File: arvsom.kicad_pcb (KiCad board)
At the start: 12 copper layers, 55 x 40 mm, 11 parts, among them J3 DF40C-100DP-0.4V(51), J4 DF40C-100DP-0.4V(51), U1 MT53D1024M32D4DT-053, U10 TDA19988BHN_C1,557, U11 KSZ9031RNXCA, U13 VIC7100, U3 MT53D1024M32D4DT-053, U8 TPS65086100, U9 GD25LQ256DWIGR

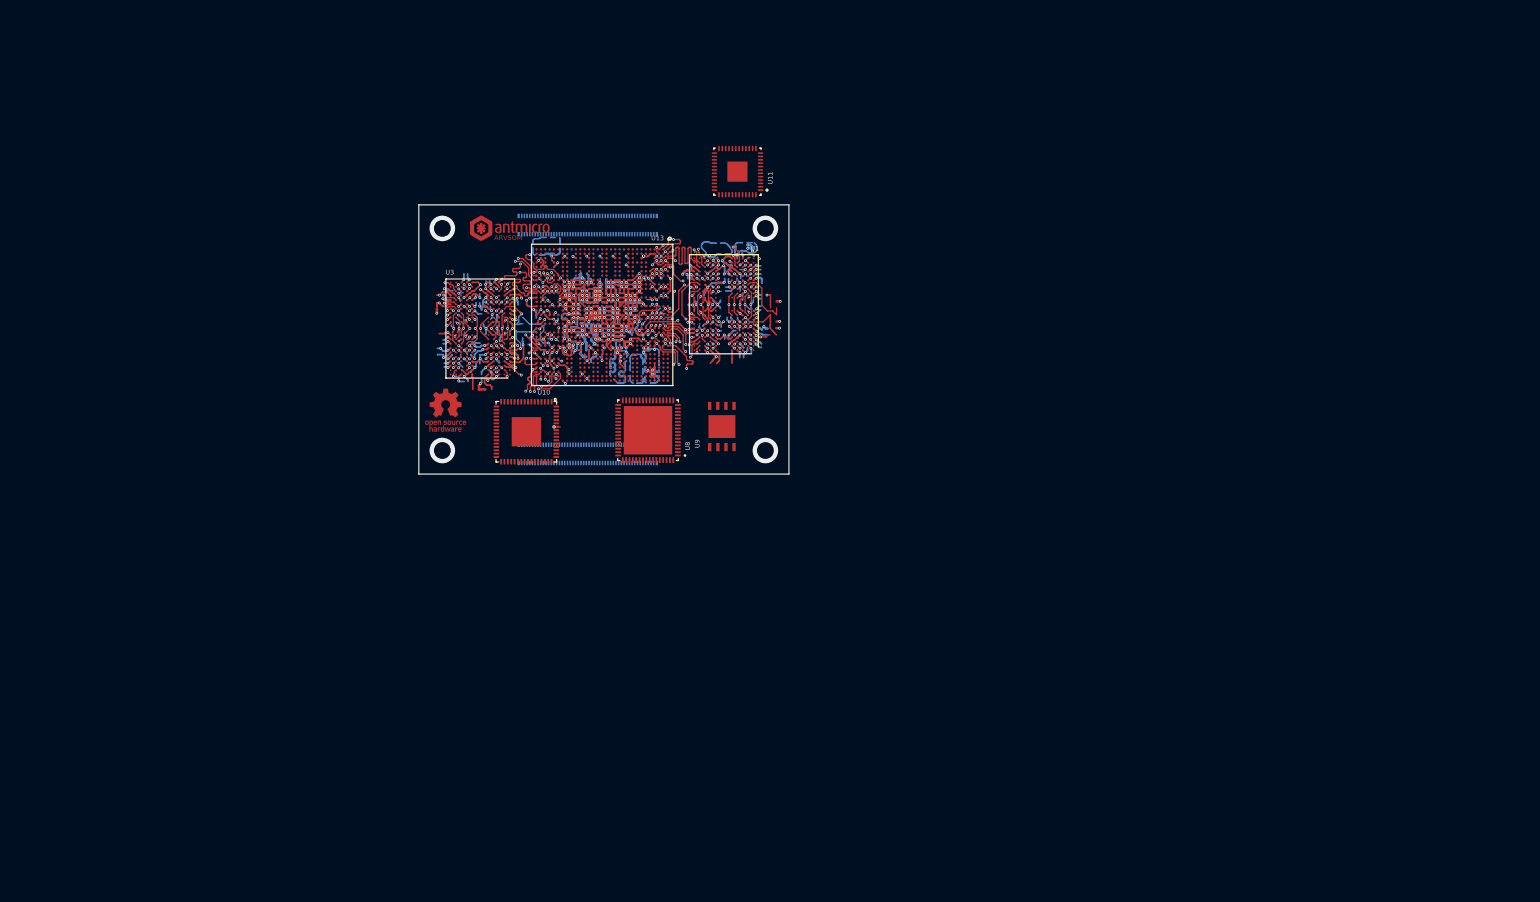
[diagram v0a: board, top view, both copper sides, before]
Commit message: Added basic rules, removed lefover zones, imported components
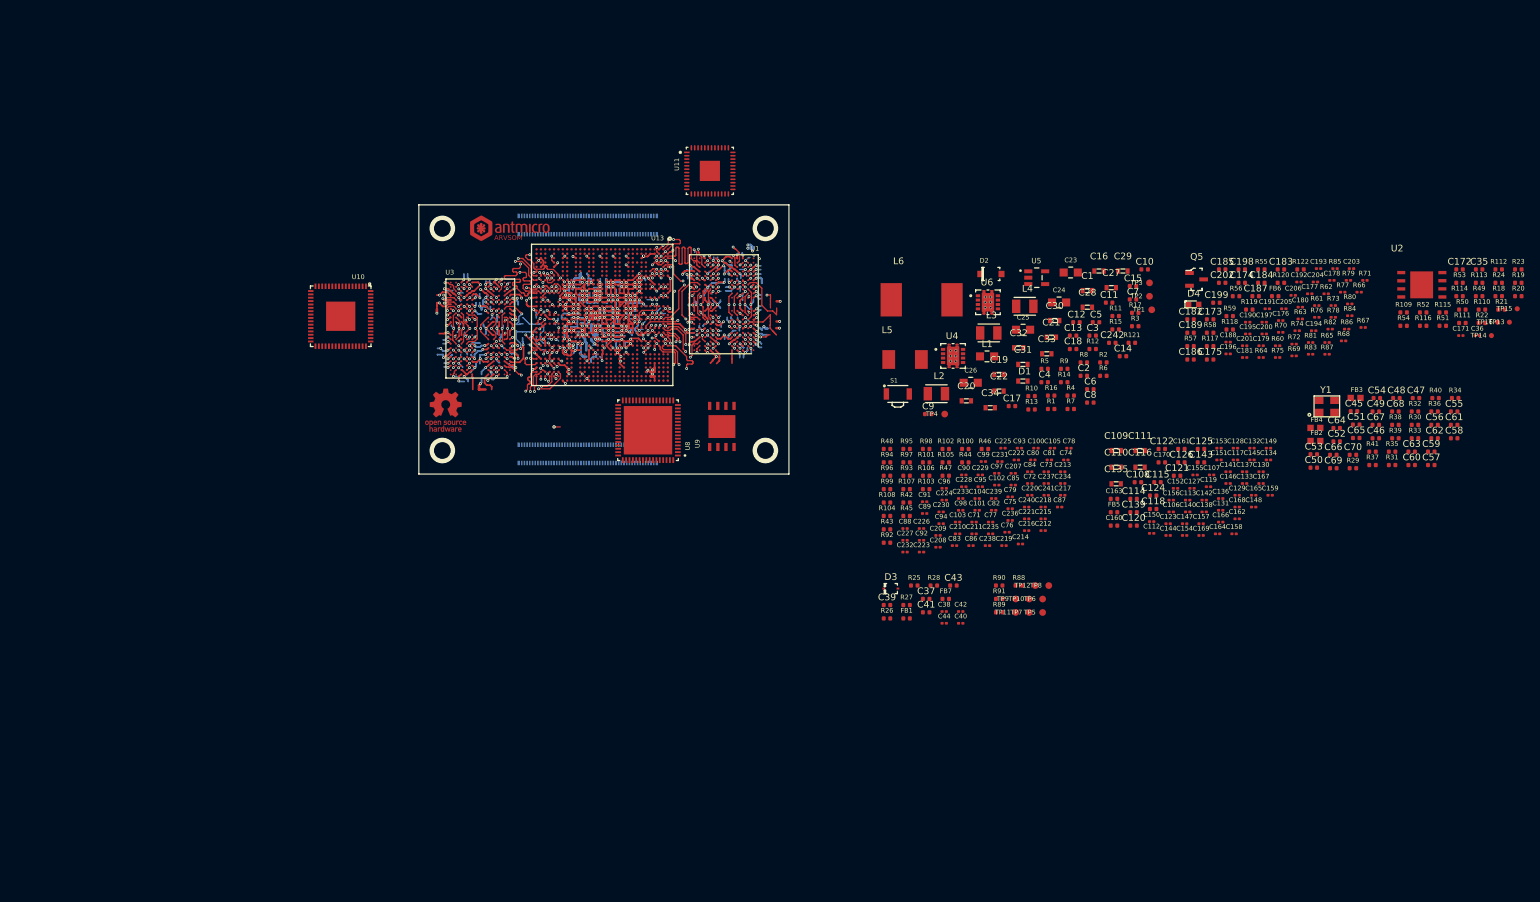
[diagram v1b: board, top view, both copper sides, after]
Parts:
- added C1: C_10u_0603, arvsom-footprints:0603-cap, F.Cu at (229.4, 67.7)
- added C10: C_100n_0402_16V, arvsom-footprints:0402-cap, F.Cu at (237.9, 64.6)
- added C100: C_100n_0201, arvsom-footprints:0201-res, F.Cu at (221.7, 91.1)
- added C101: C_100n_0201, arvsom-footprints:0201-res, F.Cu at (213.0, 100.3)
- added C102: C_100n_0201, arvsom-footprints:0201-res, F.Cu at (215.9, 96.6)
- added C103: C_100n_0201, arvsom-footprints:0201-res, F.Cu at (210.1, 102.1)
- added C104: C_100n_0201, arvsom-footprints:0201-res, F.Cu at (213.0, 98.6)
- added C105: C_100n_0201, arvsom-footprints:0201-res, F.Cu at (224.2, 91.1)
- added C106: C_100n_0201, arvsom-footprints:0201-res, F.Cu at (241.8, 100.6)
- added C107: C_100n_0201, arvsom-footprints:0201-res, F.Cu at (247.8, 95.1)
- added C108: C_1u_0402, arvsom-footprints:0402-cap, F.Cu at (236.9, 96.2)
- added C109: C_22u_0603, arvsom-footprints:0603-cap, F.Cu at (233.6, 91.5)
- added C11: C_4u7_0402, arvsom-footprints:0402-cap, F.Cu at (232.6, 69.5)
- added C110: C_22u_0603, arvsom-footprints:0603-cap, F.Cu at (233.6, 94.0)
- added C111: C_22u_0603, arvsom-footprints:0603-cap, F.Cu at (237.2, 91.5)
- added C112: C_100n_0201, arvsom-footprints:0201-res, F.Cu at (238.9, 103.8)
- added C113: C_100n_0201, arvsom-footprints:0201-res, F.Cu at (244.3, 98.8)
- added C114: C_10u_0402, arvsom-footprints:0402-cap, F.Cu at (236.2, 98.7)
- added C115: C_10u_0402, arvsom-footprints:0402-cap, F.Cu at (239.8, 96.2)
- added C116: C_22u_0603, arvsom-footprints:0603-cap, F.Cu at (237.2, 94.0)
- added C117: C_100n_0201, arvsom-footprints:0201-res, F.Cu at (251.4, 92.9)
- added C118: C_10u_0402, arvsom-footprints:0402-cap, F.Cu at (239.1, 100.2)
- added C119: C_100n_0201, arvsom-footprints:0201-res, F.Cu at (247.4, 96.8)
- added C12: C_1n0_0402, arvsom-footprints:0402-cap, F.Cu at (227.7, 72.4)
- added C120: C_10u_0402, arvsom-footprints:0402-cap, F.Cu at (236.2, 102.6)
- added C121: C_10u_0402, arvsom-footprints:0402-cap, F.Cu at (242.7, 95.2)
- added C122: C_10u_0402, arvsom-footprints:0402-cap, F.Cu at (240.4, 91.2)
- added C123: C_100n_0201, arvsom-footprints:0201-res, F.Cu at (241.4, 102.3)
- added C124: C_1u_0402, arvsom-footprints:0402-cap, F.Cu at (239.1, 98.2)
- added C125: C_1u_0402, arvsom-footprints:0402-cap, F.Cu at (246.2, 91.2)
- added C126: C_1u_0402, arvsom-footprints:0402-cap, F.Cu at (243.3, 93.2)
- added C127: C_100n_0201, arvsom-footprints:0201-res, F.Cu at (244.9, 97.1)
- added C128: C_100n_0201, arvsom-footprints:0201-res, F.Cu at (251.4, 91.1)
- added C129: C_100n_0201, arvsom-footprints:0201-res, F.Cu at (251.6, 98.1)
- added C13: C_100n_0402_16V, arvsom-footprints:0402-cap, F.Cu at (227.2, 74.4)
- added C130: C_100n_0201, arvsom-footprints:0201-res, F.Cu at (255.2, 94.6)
- added C131: C_100n_0201, arvsom-footprints:0201-res, F.Cu at (249.2, 100.3)
- added C132: C_100n_0201, arvsom-footprints:0201-res, F.Cu at (253.8, 91.1)
- added C133: C_100n_0201, arvsom-footprints:0201-res, F.Cu at (252.7, 96.4)
- added C134: C_100n_0201, arvsom-footprints:0201-res, F.Cu at (256.3, 92.9)
- added C135: C_22u_0603, arvsom-footprints:0603-cap, F.Cu at (233.6, 96.4)
- added C136: C_100n_0201, arvsom-footprints:0201-res, F.Cu at (249.2, 98.6)
- added C137: C_100n_0201, arvsom-footprints:0201-res, F.Cu at (252.7, 94.6)
- added C138: C_100n_0201, arvsom-footprints:0201-res, F.Cu at (246.7, 100.6)
- added C139: C_10u_0402, arvsom-footprints:0402-cap, F.Cu at (236.2, 100.6)
- added C14: C_4u7_0402, arvsom-footprints:0402-cap, F.Cu at (234.7, 77.5)
- added C140: C_100n_0201, arvsom-footprints:0201-res, F.Cu at (244.3, 100.6)
- added C141: C_100n_0201, arvsom-footprints:0201-res, F.Cu at (250.3, 94.6)
- added C142: C_100n_0201, arvsom-footprints:0201-res, F.Cu at (246.7, 98.8)
- added C143: C_1u_0402, arvsom-footprints:0402-cap, F.Cu at (246.2, 93.2)
- added C144: C_100n_0201, arvsom-footprints:0201-res, F.Cu at (241.4, 104.1)
- added C145: C_100n_0201, arvsom-footprints:0201-res, F.Cu at (253.8, 92.9)
- added C146: C_100n_0201, arvsom-footprints:0201-res, F.Cu at (250.3, 96.4)
- added C147: C_100n_0201, arvsom-footprints:0201-res, F.Cu at (243.8, 102.3)
- added C148: C_100n_0201, arvsom-footprints:0201-res, F.Cu at (254.1, 99.9)
- added C149: C_100n_0201, arvsom-footprints:0201-res, F.Cu at (256.3, 91.1)
- added C15: C_2u2_0402, arvsom-footprints:0402-cap, F.Cu at (236.1, 67.0)
- added C150: C_100n_0201, arvsom-footprints:0201-res, F.Cu at (238.9, 102.0)
- added C151: C_100n_0201, arvsom-footprints:0201-res, F.Cu at (248.9, 92.9)
- added C152: C_100n_0201, arvsom-footprints:0201-res, F.Cu at (242.5, 97.1)
- added C153: C_100n_0201, arvsom-footprints:0201-res, F.Cu at (248.9, 91.1)
- added C154: C_100n_0201, arvsom-footprints:0201-res, F.Cu at (243.8, 104.1)
- added C155: C_100n_0201, arvsom-footprints:0201-res, F.Cu at (245.4, 95.1)
- added C156: C_100n_0201, arvsom-footprints:0201-res, F.Cu at (241.8, 98.8)
- added C157: C_100n_0201, arvsom-footprints:0201-res, F.Cu at (246.3, 102.3)
- added C158: C_100n_0201, arvsom-footprints:0201-res, F.Cu at (251.2, 103.8)
- added C159: C_100n_0201, arvsom-footprints:0201-res, F.Cu at (256.5, 98.1)
- added C16: C_10u_0603, arvsom-footprints:0603-cap, F.Cu at (231.1, 64.8)
- added C160: C_1n_0402, arvsom-footprints:0402-res, F.Cu at (233.3, 102.6)
- added C161: C_1n_0402, arvsom-footprints:0402-res, F.Cu at (243.3, 91.2)
- added C162: C_100n_0201, arvsom-footprints:0201-res, F.Cu at (251.6, 101.6)
- added C163: C_1n_0402, arvsom-footprints:0402-res, F.Cu at (233.3, 98.7)
- added C164: C_100n_0201, arvsom-footprints:0201-res, F.Cu at (248.7, 103.8)
- added C165: C_100n_0201, arvsom-footprints:0201-res, F.Cu at (254.1, 98.1)
- added C166: C_100n_0201, arvsom-footprints:0201-res, F.Cu at (249.2, 102.1)
- added C167: C_100n_0201, arvsom-footprints:0201-res, F.Cu at (255.2, 96.4)
- added C168: C_100n_0201, arvsom-footprints:0201-res, F.Cu at (251.6, 99.9)
- added C169: C_100n_0201, arvsom-footprints:0201-res, F.Cu at (246.3, 104.1)
- added C17: C_100n_0402_16V, arvsom-footprints:0402-cap, F.Cu at (218.2, 84.9)
- added C170: C_1n_0402, arvsom-footprints:0402-res, F.Cu at (240.4, 93.2)
- added C171: C_100n_0201, arvsom-footprints:0201-res, F.Cu at (284.9, 74.4)
- added C172: C_10n_0402, arvsom-footprints:0402-cap, F.Cu at (284.7, 64.6)
- added C173: C_1u_0402, arvsom-footprints:0402-cap, F.Cu at (247.6, 72.0)
- added C174: C_1u_0402, arvsom-footprints:0402-cap, F.Cu at (252.3, 66.5)
- added C175: C_1u_0402, arvsom-footprints:0402-cap, F.Cu at (247.6, 78.0)
- added C176: C_100n_0201, arvsom-footprints:0201-res, F.Cu at (258.1, 72.2)
- added C177: C_100n_0201, arvsom-footprints:0201-res, F.Cu at (262.4, 68.2)
- added C178: C_100n_0201, arvsom-footprints:0201-res, F.Cu at (265.7, 66.2)
- added C179: C_100n_0201, arvsom-footprints:0201-res, F.Cu at (255.2, 75.9)
- added C18: C_100n_0402_16V, arvsom-footprints:0402-cap, F.Cu at (227.2, 76.4)
- added C180: C_100n_0201, arvsom-footprints:0201-res, F.Cu at (261.0, 70.2)
- added C181: C_100n_0201, arvsom-footprints:0201-res, F.Cu at (252.7, 77.7)
- added C182: C_10u_0402, arvsom-footprints:0402-cap, F.Cu at (244.7, 72.0)
- added C183: C_1u_0402, arvsom-footprints:0402-cap, F.Cu at (258.1, 64.6)
- added C184: C_10u_0402, arvsom-footprints:0402-cap, F.Cu at (255.2, 66.5)
- added C185: C_1u_0402, arvsom-footprints:0402-cap, F.Cu at (249.4, 64.6)
- added C186: C_1u_0402, arvsom-footprints:0402-cap, F.Cu at (244.7, 78.0)
- added C187: C_1u_0402, arvsom-footprints:0402-cap, F.Cu at (254.4, 68.5)
- added C188: C_100n_0201, arvsom-footprints:0201-res, F.Cu at (250.3, 75.4)
- added C189: C_1u_0402, arvsom-footprints:0402-cap, F.Cu at (244.7, 74.0)
- added C19: C_22u_0603, arvsom-footprints:0603-cap, F.Cu at (216.2, 80.2)
- added C190: C_100n_0201, arvsom-footprints:0201-res, F.Cu at (253.2, 72.4)
- added C191: C_100n_0201, arvsom-footprints:0201-res, F.Cu at (256.1, 70.4)
- added C192: C_100n_0201, arvsom-footprints:0201-res, F.Cu at (260.8, 66.4)
- added C193: C_100n_0201, arvsom-footprints:0201-res, F.Cu at (263.7, 64.4)
- added C194: C_100n_0201, arvsom-footprints:0201-res, F.Cu at (263.0, 73.7)
- added C195: C_100n_0201, arvsom-footprints:0201-res, F.Cu at (253.2, 74.2)
- added C196: C_100n_0201, arvsom-footprints:0201-res, F.Cu at (250.3, 77.1)
- added C197: C_100n_0201, arvsom-footprints:0201-res, F.Cu at (255.6, 72.4)
- added C198: C_1u_0402, arvsom-footprints:0402-cap, F.Cu at (252.3, 64.6)
- added C199: C_1u_0402, arvsom-footprints:0402-cap, F.Cu at (248.5, 69.5)
- added C2: C_2u2_0402, arvsom-footprints:0402-cap, F.Cu at (228.8, 80.4)
- added C20: C_22u_0603, arvsom-footprints:0603-cap, F.Cu at (211.4, 84.1)
- added C200: C_100n_0201, arvsom-footprints:0201-res, F.Cu at (255.6, 74.2)
- added C201: C_100n_0201, arvsom-footprints:0201-res, F.Cu at (252.7, 75.9)
- added C202: C_1u_0402, arvsom-footprints:0402-cap, F.Cu at (249.4, 66.5)
- added C203: C_100n_0201, arvsom-footprints:0201-res, F.Cu at (268.6, 64.4)
- added C204: C_100n_0201, arvsom-footprints:0201-res, F.Cu at (263.2, 66.4)
- added C205: C_100n_0201, arvsom-footprints:0201-res, F.Cu at (258.6, 70.4)
- added C206: C_100n_0201, arvsom-footprints:0201-res, F.Cu at (259.9, 68.4)
- added C207: C_100n_0201, arvsom-footprints:0201-res, F.Cu at (218.3, 94.9)
- added C208: C_100n_0201, arvsom-footprints:0201-res, F.Cu at (207.2, 105.8)
- added C209: C_100n_0201, arvsom-footprints:0201-res, F.Cu at (207.2, 104.1)
- added C21: C_22u_0603, arvsom-footprints:0603-cap, F.Cu at (224.0, 74.6)
- added C210: C_100n_0201, arvsom-footprints:0201-res, F.Cu at (210.1, 103.8)
- added C211: C_100n_0201, arvsom-footprints:0201-res, F.Cu at (212.5, 103.8)
- added C212: C_100n_0201, arvsom-footprints:0201-res, F.Cu at (222.8, 103.4)
- added C213: C_100n_0201, arvsom-footprints:0201-res, F.Cu at (225.7, 94.6)
- added C214: C_100n_0201, arvsom-footprints:0201-res, F.Cu at (219.4, 105.4)
- added C215: C_100n_0201, arvsom-footprints:0201-res, F.Cu at (222.8, 101.6)
- added C216: C_100n_0201, arvsom-footprints:0201-res, F.Cu at (220.3, 103.4)
- added C217: C_100n_0201, arvsom-footprints:0201-res, F.Cu at (225.7, 98.1)
- added C218: C_100n_0201, arvsom-footprints:0201-res, F.Cu at (222.8, 99.9)
- added C219: C_100n_0201, arvsom-footprints:0201-res, F.Cu at (217.0, 105.6)
- added C22: C_22u_0603, arvsom-footprints:0603-cap, F.Cu at (216.2, 82.6)
- added C220: C_100n_0201, arvsom-footprints:0201-res, F.Cu at (220.8, 98.1)
- added C221: C_100n_0201, arvsom-footprints:0201-res, F.Cu at (220.3, 101.6)
- added C222: C_100n_0201, arvsom-footprints:0201-res, F.Cu at (218.8, 92.9)
- added C223: C_100n_0201, arvsom-footprints:0201-res, F.Cu at (204.7, 106.6)
- added C224: C_100n_0201, arvsom-footprints:0201-res, F.Cu at (208.1, 98.8)
- added C225: C_100n_0201, arvsom-footprints:0201-res, F.Cu at (216.8, 91.1)
- added C226: C_100n_0201, arvsom-footprints:0201-res, F.Cu at (204.7, 103.1)
- added C227: C_100n_0201, arvsom-footprints:0201-res, F.Cu at (202.3, 104.8)
- added C228: C_100n_0201, arvsom-footprints:0201-res, F.Cu at (211.0, 96.8)
- added C229: C_100n_0201, arvsom-footprints:0201-res, F.Cu at (213.4, 95.1)
- added C23: C_100u_0805, arvsom-footprints:0805-cap, F.Cu at (226.9, 65.0)
- added C230: C_100n_0201, arvsom-footprints:0201-res, F.Cu at (207.6, 100.6)
- added C231: C_100n_0201, arvsom-footprints:0201-res, F.Cu at (216.4, 93.1)
- added C232: C_100n_0201, arvsom-footprints:0201-res, F.Cu at (202.3, 106.6)
- added C233: C_100n_0201, arvsom-footprints:0201-res, F.Cu at (210.5, 98.6)
- added C234: C_100n_0201, arvsom-footprints:0201-res, F.Cu at (225.7, 96.4)
- added C235: C_100n_0201, arvsom-footprints:0201-res, F.Cu at (215.0, 103.8)
- added C236: C_100n_0201, arvsom-footprints:0201-res, F.Cu at (217.9, 101.9)
- added C237: C_100n_0201, arvsom-footprints:0201-res, F.Cu at (223.2, 96.4)
- added C238: C_100n_0201, arvsom-footprints:0201-res, F.Cu at (214.5, 105.6)
- added C239: C_100n_0201, arvsom-footprints:0201-res, F.Cu at (215.4, 98.6)
- added C24: C_100u_0805, arvsom-footprints:0805-cap, F.Cu at (225.2, 69.5)
- added C240: C_100n_0201, arvsom-footprints:0201-res, F.Cu at (220.3, 99.9)
- added C241: C_100n_0201, arvsom-footprints:0201-res, F.Cu at (223.2, 98.1)
- added C242: C_100n_0402_16V, arvsom-footprints:0402-cap, F.Cu at (233.1, 75.5)
- added C25: C_100u_0805, arvsom-footprints:0805-cap, F.Cu at (219.8, 73.5)
- added C26: C_100u_0805, arvsom-footprints:0805-cap, F.Cu at (212.0, 81.4)
- added C27: C_10u_0603, arvsom-footprints:0603-cap, F.Cu at (232.9, 67.3)
- added C28: C_10u_0603, arvsom-footprints:0603-cap, F.Cu at (229.4, 70.2)
- added C29: C_22u_0603, arvsom-footprints:0603-cap, F.Cu at (234.6, 64.8)
- added C3: C_10u_0402, arvsom-footprints:0402-cap, F.Cu at (230.2, 74.4)
- added C30: C_22u_0603, arvsom-footprints:0603-cap, F.Cu at (224.5, 72.2)
- added C31: C_22u_0603, arvsom-footprints:0603-cap, F.Cu at (219.8, 78.7)
- added C32: C_22u_0603, arvsom-footprints:0603-cap, F.Cu at (219.2, 76.2)
- added C33: C_22u_0603, arvsom-footprints:0603-cap, F.Cu at (223.3, 77.1)
- added C34: C_22u_0603, arvsom-footprints:0603-cap, F.Cu at (214.9, 85.1)
- added C35: C_1u_0402, arvsom-footprints:0402-cap, F.Cu at (287.6, 64.6)
- added C36: C_100n_0201, arvsom-footprints:0201-res, F.Cu at (287.3, 74.4)
- added C37: C_2u2_0402, arvsom-footprints:0402-cap, F.Cu at (205.4, 113.5)
- added C38: C_100n_0201, arvsom-footprints:0201-res, F.Cu at (208.1, 115.4)
- added C39: C_2u2_0402, arvsom-footprints:0402-cap, F.Cu at (199.6, 114.4)
- added C4: C_10u_0402, arvsom-footprints:0402-cap, F.Cu at (223.0, 81.3)
- added C40: C_100n_0201, arvsom-footprints:0201-res, F.Cu at (210.5, 117.1)
- added C41: C_2u2_0402, arvsom-footprints:0402-cap, F.Cu at (205.4, 115.5)
- added C42: C_100n_0201, arvsom-footprints:0201-res, F.Cu at (210.5, 115.4)
- added C43: C_2u2_0402, arvsom-footprints:0402-cap, F.Cu at (209.5, 111.5)
- added C44: C_100n_0201, arvsom-footprints:0201-res, F.Cu at (208.1, 117.1)
- added C45: C_4u7_0402, arvsom-footprints:0402-cap, F.Cu at (269.0, 85.6)
- added C46: C_470n_0402, arvsom-footprints:0402-cap, F.Cu at (272.2, 89.7)
- added C47: C_4u7_0402, arvsom-footprints:0402-cap, F.Cu at (278.2, 83.7)
- added C48: C_470n_0402, arvsom-footprints:0402-cap, F.Cu at (275.3, 83.7)
- added C49: C_4u7_0402, arvsom-footprints:0402-cap, F.Cu at (272.2, 85.7)
- added C5: C_2u2_0402, arvsom-footprints:0402-cap, F.Cu at (230.7, 72.4)
- added C50: C_4u7_0402, arvsom-footprints:0402-cap, F.Cu at (263.0, 94.0)
- added C51: C_470n_0402, arvsom-footprints:0402-cap, F.Cu at (269.3, 87.6)
- added C52: C_470n_0402, arvsom-footprints:0402-cap, F.Cu at (266.4, 90.1)
- added C53: C_470n_0402, arvsom-footprints:0402-cap, F.Cu at (263.0, 92.0)
- added C54: C_100n_0402, arvsom-footprints:0402-cap, F.Cu at (272.4, 83.7)
- added C55: C_10n_0402, arvsom-footprints:0402-cap, F.Cu at (283.9, 85.7)
- added C56: C_10n_0402, arvsom-footprints:0402-cap, F.Cu at (280.9, 87.7)
- added C57: C_10n_0402, arvsom-footprints:0402-cap, F.Cu at (280.5, 93.6)
- added C58: C_4u7_0402, arvsom-footprints:0402-cap, F.Cu at (283.9, 89.7)
- added C59: C_10n_0402, arvsom-footprints:0402-cap, F.Cu at (280.5, 91.6)
- added C6: C_4u7_0402, arvsom-footprints:0402-cap, F.Cu at (229.8, 82.4)
- added C60: C_10n_0402, arvsom-footprints:0402-cap, F.Cu at (277.6, 93.6)
- added C61: C_10n_0402, arvsom-footprints:0402-cap, F.Cu at (283.9, 87.7)
- added C62: C_10n_0402, arvsom-footprints:0402-cap, F.Cu at (280.9, 89.7)
- added C63: C_10n_0402, arvsom-footprints:0402-cap, F.Cu at (277.6, 91.6)
- added C64: C_10n_0402, arvsom-footprints:0402-cap, F.Cu at (266.4, 88.1)
- added C65: C_10n_0402, arvsom-footprints:0402-cap, F.Cu at (269.3, 89.6)
- added C66: C_10n_0402, arvsom-footprints:0402-cap, F.Cu at (265.9, 92.1)
- added C67: C_10n_0402, arvsom-footprints:0402-cap, F.Cu at (272.2, 87.7)
- added C68: C_10n_0402, arvsom-footprints:0402-cap, F.Cu at (275.1, 85.7)
- added C69: C_22p_0402, arvsom-footprints:0402-cap, F.Cu at (265.9, 94.1)
- added C7: C_2u2_0402, arvsom-footprints:0402-cap, F.Cu at (236.1, 69.0)
- added C70: C_22p_0402, arvsom-footprints:0402-cap, F.Cu at (268.8, 92.1)
- added C71: C_100n_0201, arvsom-footprints:0201-res, F.Cu at (212.5, 102.1)
- added C72: C_100n_0201, arvsom-footprints:0201-res, F.Cu at (220.8, 96.4)
- added C73: C_100n_0201, arvsom-footprints:0201-res, F.Cu at (223.2, 94.6)
- added C74: C_100n_0201, arvsom-footprints:0201-res, F.Cu at (226.2, 92.9)
- added C75: C_100n_0201, arvsom-footprints:0201-res, F.Cu at (217.9, 100.1)
- added C76: C_100n_0201, arvsom-footprints:0201-res, F.Cu at (217.4, 103.6)
- added C77: C_100n_0201, arvsom-footprints:0201-res, F.Cu at (215.0, 102.1)
- added C78: C_100n_0201, arvsom-footprints:0201-res, F.Cu at (226.6, 91.1)
- added C79: C_100n_0201, arvsom-footprints:0201-res, F.Cu at (217.9, 98.4)
- added C8: C_10u_0402, arvsom-footprints:0402-cap, F.Cu at (229.8, 84.3)
- added C80: C_100n_0201, arvsom-footprints:0201-res, F.Cu at (221.3, 92.9)
- added C81: C_100n_0201, arvsom-footprints:0201-res, F.Cu at (223.7, 92.9)
- added C82: C_100n_0201, arvsom-footprints:0201-res, F.Cu at (215.4, 100.3)
- added C83: C_100n_0201, arvsom-footprints:0201-res, F.Cu at (209.6, 105.6)
- added C84: C_100n_0201, arvsom-footprints:0201-res, F.Cu at (220.8, 94.6)
- added C85: C_100n_0201, arvsom-footprints:0201-res, F.Cu at (218.3, 96.6)
- added C86: C_100n_0201, arvsom-footprints:0201-res, F.Cu at (212.1, 105.6)
- added C87: C_100n_0201, arvsom-footprints:0201-res, F.Cu at (225.2, 99.9)
- added C88: C_100n_0201, arvsom-footprints:0201-res, F.Cu at (202.3, 103.1)
- added C89: C_100n_0201, arvsom-footprints:0201-res, F.Cu at (205.2, 100.8)
- added C9: C_2u2_0402, arvsom-footprints:0402-cap, F.Cu at (205.7, 86.0)
- added C90: C_100n_0201, arvsom-footprints:0201-res, F.Cu at (211.0, 95.1)
- added C91: C_100n_0201, arvsom-footprints:0201-res, F.Cu at (205.2, 99.1)
- added C92: C_100n_0201, arvsom-footprints:0201-res, F.Cu at (204.7, 104.8)
- added C93: C_100n_0201, arvsom-footprints:0201-res, F.Cu at (219.3, 91.1)
- added C94: C_100n_0201, arvsom-footprints:0201-res, F.Cu at (207.6, 102.3)
- added C95: C_100n_0201, arvsom-footprints:0201-res, F.Cu at (213.4, 96.8)
- added C96: C_100n_0201, arvsom-footprints:0201-res, F.Cu at (208.1, 97.1)
- added C97: C_100n_0201, arvsom-footprints:0201-res, F.Cu at (215.9, 94.9)
- added C98: C_100n_0201, arvsom-footprints:0201-res, F.Cu at (210.5, 100.3)
- added C99: C_100n_0201, arvsom-footprints:0201-res, F.Cu at (213.9, 93.1)
- added D1: PGB1010603MR, arvsom-footprints:PGB1010603MR, F.Cu at (219.8, 81.2)
- added D2: 1N4148W-TP, arvsom-footprints:SOD-123, F.Cu at (215.0, 65.2)
- added D3: 1N4148WS, arvsom-footprints:SOD-323F, F.Cu at (200.2, 112.0)
- added D4: KP-1608CGCK, arvsom-footprints:LED_0603, F.Cu at (245.2, 69.8)
- added FB1: BLM15PD121SN1D, arvsom-footprints:0402-res, F.Cu at (202.5, 116.4)
- added FB2: BLM18AG601SN1D, arvsom-footprints:0603, F.Cu at (263.2, 90.1)
- added FB3: BLM18AG601SN1D, arvsom-footprints:0603, F.Cu at (269.2, 83.7)
- added FB4: BLM18AG601SN1D, arvsom-footprints:0603, F.Cu at (263.2, 88.1)
- added FB5: BLM15PD121SN1D, arvsom-footprints:0402-res, F.Cu at (233.3, 100.6)
- added FB6: BLM15PD121SN1D, arvsom-footprints:0402-res, F.Cu at (257.3, 68.5)
- added FB7: BLM15PD121SN1D, arvsom-footprints:0402-res, F.Cu at (208.3, 113.5)
- added L1: 10uH, arvsom-footprints:0805-res, F.Cu at (214.5, 77.5)
- added L2: LQH32PN1R0NN0L, arvsom-footprints:IND_LQH32PN1R0NN0L, F.Cu at (206.9, 83.0)
- added L3: LQH32PN1R0NN0L, arvsom-footprints:IND_LQH32PN1R0NN0L, F.Cu at (214.7, 74.0)
- added L4: LQH32PN1R0NN0L, arvsom-footprints:IND_LQH32PN1R0NN0L, F.Cu at (220.1, 70.0)
- added L5: MPX1D0520LR47, arvsom-footprints:MPX1D0520LR47, F.Cu at (198.9, 76.5)
- added L6: IHLP4040DZERR56M01, arvsom-footprints:IHLP4040DZERR56M01, F.Cu at (199.3, 67.6)
- added Q5: BSS138AKA, arvsom-footprints:SOT-23-3, F.Cu at (245.6, 66.0)
- added R1: R_1M0_0402, arvsom-footprints:0402-res, F.Cu at (224.0, 85.3)
- added R10: R_0R_0402, arvsom-footprints:0402-res, F.Cu at (221.1, 83.4)
- added R100: R_0R_0402, arvsom-footprints:0402-res, F.Cu at (211.2, 91.2)
- added R101: R_10k_0402, arvsom-footprints:0402-res, F.Cu at (205.4, 93.2)
- added R102: R_0R_0402, arvsom-footprints:0402-res, F.Cu at (208.3, 91.2)
- added R103: R_10k_0402, arvsom-footprints:0402-res, F.Cu at (205.4, 97.2)
- added R104: R_10k_0402, arvsom-footprints:0402-res, F.Cu at (199.6, 101.2)
- added R105: R_10k_0402, arvsom-footprints:0402-res, F.Cu at (208.3, 93.2)
- added R106: R_10k_0402, arvsom-footprints:0402-res, F.Cu at (205.4, 95.2)
- added R107: R_10k_0402, arvsom-footprints:0402-res, F.Cu at (202.5, 97.2)
- added R108: R_10k_0402, arvsom-footprints:0402-res, F.Cu at (199.6, 99.2)
- added R109: R_10k_0402, arvsom-footprints:0402-res, F.Cu at (276.4, 71.0)
- added R11: R_0R_0402, arvsom-footprints:0402-res, F.Cu at (233.6, 71.5)
- added R110: R_10k_0402, arvsom-footprints:0402-res, F.Cu at (288.0, 70.5)
- added R111: R_10k_0402, arvsom-footprints:0402-res, F.Cu at (285.1, 72.5)
- added R112: R_10k_0402, arvsom-footprints:0402-res, F.Cu at (290.5, 64.6)
- added R113: R_10k_0402, arvsom-footprints:0402-res, F.Cu at (287.6, 66.5)
- added R114: R_10k_0402, arvsom-footprints:0402-res, F.Cu at (284.7, 68.5)
- added R115: R_10k_0402, arvsom-footprints:0402-res, F.Cu at (282.2, 71.0)
- added R116: R_10k_0402, arvsom-footprints:0402-res, F.Cu at (279.3, 72.9)
- added R117: R_2k_0402, arvsom-footprints:0402-res, F.Cu at (247.6, 76.0)
- added R118: R_2k_0402, arvsom-footprints:0402-res, F.Cu at (250.5, 73.5)
- added R119: R_33R_0402, arvsom-footprints:0402-res, F.Cu at (253.4, 70.5)
- added R12: R_0R_0402, arvsom-footprints:0402-res, F.Cu at (230.2, 76.4)
- added R120: R_1k_0402, arvsom-footprints:0402-res, F.Cu at (258.1, 66.5)
- added R121: R_10k_0402, arvsom-footprints:0402-res, F.Cu at (236.0, 75.5)
- added R122: R_10k_0402, arvsom-footprints:0402-res, F.Cu at (261.0, 64.6)
- added R13: R_4k7_0402, arvsom-footprints:0402-res, F.Cu at (221.1, 85.4)
- added R14: R_0R_0402, arvsom-footprints:0402-res, F.Cu at (225.9, 81.3)
- added R15: R_0R_0402, arvsom-footprints:0402-res, F.Cu at (233.6, 73.5)
- added R16: R_0R_0402, arvsom-footprints:0402-res, F.Cu at (224.0, 83.3)
- added R17: R_4k7_0402, arvsom-footprints:0402-res, F.Cu at (236.5, 71.0)
- added R18: R_33R_0402, arvsom-footprints:0402-res, F.Cu at (290.5, 68.5)
- added R19: R_33R_0402, arvsom-footprints:0402-res, F.Cu at (293.4, 66.5)
- added R2: R_10k_0402, arvsom-footprints:0402-res, F.Cu at (231.7, 78.4)
- added R20: R_33R_0402, arvsom-footprints:0402-res, F.Cu at (293.4, 68.5)
- added R21: R_4k7_0402, arvsom-footprints:0402-res, F.Cu at (290.9, 70.5)
- added R22: R_33R_0402, arvsom-footprints:0402-res, F.Cu at (288.0, 72.5)
- added R23: R_33R_0402, arvsom-footprints:0402-res, F.Cu at (293.4, 64.6)
- added R24: R_33R_0402, arvsom-footprints:0402-res, F.Cu at (290.5, 66.5)
- added R25: R_10k_0402, arvsom-footprints:0402-res, F.Cu at (203.6, 111.5)
- added R26: R_1k_0402, arvsom-footprints:0402-res, F.Cu at (199.6, 116.4)
- added R27: R_1k_0402, arvsom-footprints:0402-res, F.Cu at (202.5, 114.4)
- added R28: R_27k_0402, arvsom-footprints:0402-res, F.Cu at (206.6, 111.5)
- added R29: R_1k_0402, arvsom-footprints:0402-res, F.Cu at (268.8, 94.1)
- added R3: R_10k_0402, arvsom-footprints:0402-res, F.Cu at (236.5, 73.0)
- added R30: R_12k1_0402, arvsom-footprints:0402-res, F.Cu at (278.0, 87.7)
- added R31: R_10k_0402, arvsom-footprints:0402-res, F.Cu at (274.6, 93.6)
- added R32: R_10k_0402, arvsom-footprints:0402-res, F.Cu at (278.0, 85.7)
- added R33: R_10k_0402, arvsom-footprints:0402-res, F.Cu at (278.0, 89.7)
- added R34: R_10k_0402, arvsom-footprints:0402-res, F.Cu at (284.0, 83.7)
- added R35: R_10k_0402, arvsom-footprints:0402-res, F.Cu at (274.6, 91.6)
- added R36: R_10k_0402, arvsom-footprints:0402-res, F.Cu at (280.9, 85.7)
- added R37: R_4k7_0402, arvsom-footprints:0402-res, F.Cu at (271.7, 93.6)
- added R38: R_10k_0402, arvsom-footprints:0402-res, F.Cu at (275.1, 87.7)
- added R39: R_10k_0402, arvsom-footprints:0402-res, F.Cu at (275.1, 89.7)
- added R4: R_10k_0402, arvsom-footprints:0402-res, F.Cu at (226.9, 83.3)
- added R40: R_10k_0402, arvsom-footprints:0402-res, F.Cu at (281.1, 83.7)
- added R41: R_1M5_0402, arvsom-footprints:0402-res, F.Cu at (271.7, 91.6)
- added R42: R_240R_0402, arvsom-footprints:0402-res, F.Cu at (202.5, 99.2)
- added R43: R_10k_0402, arvsom-footprints:0402-res, F.Cu at (199.6, 103.2)
- added R44: R_10k_0402, arvsom-footprints:0402-res, F.Cu at (211.2, 93.2)
- added R45: R_240R_0402, arvsom-footprints:0402-res, F.Cu at (202.5, 101.2)
- added R46: R_0R_0402, arvsom-footprints:0402-res, F.Cu at (214.1, 91.2)
- added R47: R_10k_0402, arvsom-footprints:0402-res, F.Cu at (208.3, 95.2)
- added R48: R_0R_0402, arvsom-footprints:0402-res, F.Cu at (199.6, 91.2)
- added R49: R_10k_0402, arvsom-footprints:0402-res, F.Cu at (287.6, 68.5)
- added R5: R_0R_0402, arvsom-footprints:0402-res, F.Cu at (223.0, 79.3)
- added R50: R_10k_0402, arvsom-footprints:0402-res, F.Cu at (285.1, 70.5)
- added R51: R_10k_0402, arvsom-footprints:0402-res, F.Cu at (282.2, 72.9)
- added R52: R_10k_0402, arvsom-footprints:0402-res, F.Cu at (279.3, 71.0)
- added R53: R_10k_0402, arvsom-footprints:0402-res, F.Cu at (284.7, 66.5)
- added R54: R_10k_0402, arvsom-footprints:0402-res, F.Cu at (276.4, 72.9)
- added R55: R_33R_0402, arvsom-footprints:0402-res, F.Cu at (255.2, 64.6)
- added R56: R_33R_0402, arvsom-footprints:0402-res, F.Cu at (251.4, 68.5)
- added R57: R_33R_0402, arvsom-footprints:0402-res, F.Cu at (244.7, 76.0)
- added R58: R_33R_0402, arvsom-footprints:0402-res, F.Cu at (247.6, 74.0)
- added R59: R_33R_0402, arvsom-footprints:0402-res, F.Cu at (250.5, 71.5)
- added R6: R_0R_0402, arvsom-footprints:0402-res, F.Cu at (231.7, 80.4)
- added R60: R_33R_0201, arvsom-footprints:0201-res, F.Cu at (257.6, 75.9)
- added R61: R_33R_0201, arvsom-footprints:0201-res, F.Cu at (263.4, 69.9)
- added R62: R_33R_0201, arvsom-footprints:0201-res, F.Cu at (264.9, 68.2)
- added R63: R_33R_0201, arvsom-footprints:0201-res, F.Cu at (261.0, 71.9)
- added R64: R_33R_0201, arvsom-footprints:0201-res, F.Cu at (255.2, 77.7)
- added R65: R_33R_0201, arvsom-footprints:0201-res, F.Cu at (265.0, 75.4)
- added R66: R_33R_0201, arvsom-footprints:0201-res, F.Cu at (269.8, 67.9)
- added R67: R_33R_0201, arvsom-footprints:0201-res, F.Cu at (270.3, 73.2)
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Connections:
- U13 pad AJ5: DDR1_DQ31 -> (no net)
- U3 pad AB4: VDDQ -> VDD2
- U3 pad B10: VDD2 -> VDDQ
- U3 pad B8: VDD2 -> VDDQ
- U3 pad F5: VDDQ -> VDD2
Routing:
- removed copper zone on B.Cu, net (none)
- removed copper zone on In2.Cu, net (none)
- removed copper zone on In4.Cu, net (none)
- removed copper zone on In7.Cu, net (none)
- removed copper zone on In9.Cu, net (none)
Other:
- net class Default: trace_width 0.11 -> 0.127; via_dia 0.8 -> 0.4; via_drill 0.4 -> 0.2
- rule trace_min: 0.11 -> 0.127
- rule via_min_drill: 0.3 -> 0.2

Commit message: Updated PMIC components. PMIC component grouping
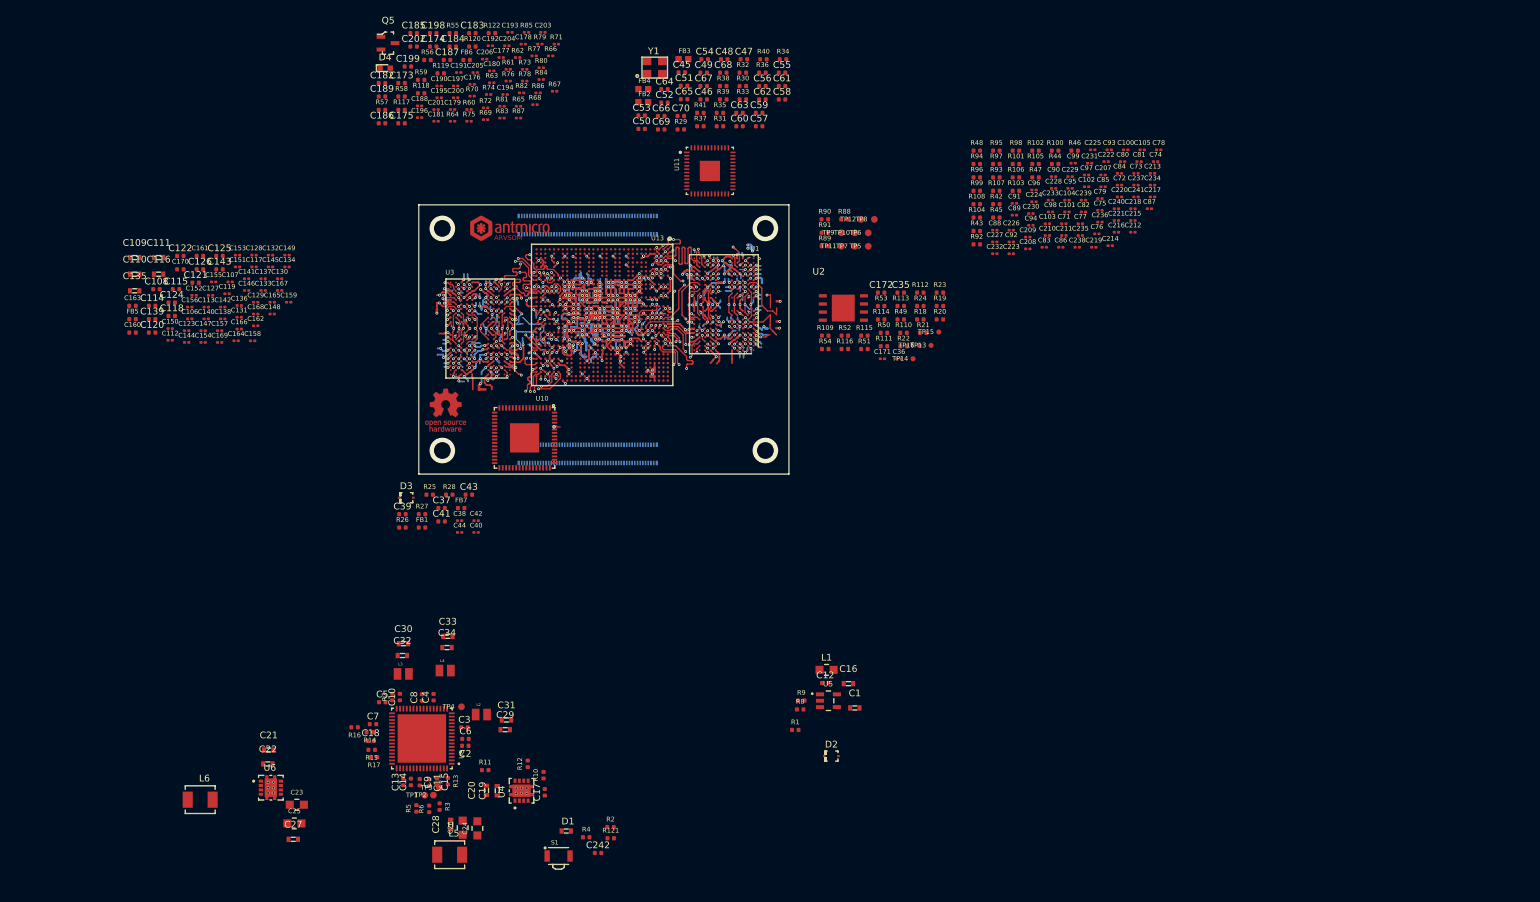
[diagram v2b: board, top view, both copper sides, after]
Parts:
- removed U9: GD25LQ256DWIGR, arvsom-footprints:8-WSON-6x5
- D2: value 1N4148W-TP -> PMEG3010CEJ; footprint arvsom-footprints:SOD-123 -> arvsom-footprints:SOD-323F
- L2, L3, L4: value LQH32PN1R0NN0L -> 1uH_2.0x1.6; footprint arvsom-footprints:IND_LQH32PN1R0NN0L -> arvsom-footprints:INDC2016X100N
- L5: value MPX1D0520LR47 -> 0.56uH_7.3A; footprint arvsom-footprints:MPX1D0520LR47 -> arvsom-footprints:SRP4020
- L6: value IHLP4040DZERR56M01 -> 0.47uH_10.5A; footprint arvsom-footprints:IHLP4040DZERR56M01 -> arvsom-footprints:SRP4020
- moved C113 148.6 mm to (98.4, 70.2)
- moved C119 148.6 mm to (101.5, 68.2)
- moved C123 148.6 mm to (95.5, 73.7)
- moved C125 148.6 mm to (100.4, 62.6)
- moved C126 148.6 mm to (97.5, 64.5)
- moved C140 148.6 mm to (98.4, 71.9)
- moved C141 148.6 mm to (104.4, 65.9)
- moved C143 148.6 mm to (100.4, 64.5)
- moved C144 148.6 mm to (95.5, 75.4)
- moved C146 148.6 mm to (104.4, 67.7)
- moved C152 148.6 mm to (96.6, 68.4)
- moved C161 148.6 mm to (97.5, 62.6)
- moved C164 148.6 mm to (102.9, 75.2)
- moved C106 148.6 mm to (96.0, 71.9)
- moved C107 148.6 mm to (102.0, 66.4)
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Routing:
- net LCD_DATA5: track 0.94 -> 0.00 mm, vias 1 -> 0
- net LCD_DATA3: track 0.00 -> 0.94 mm, vias 0 -> 1

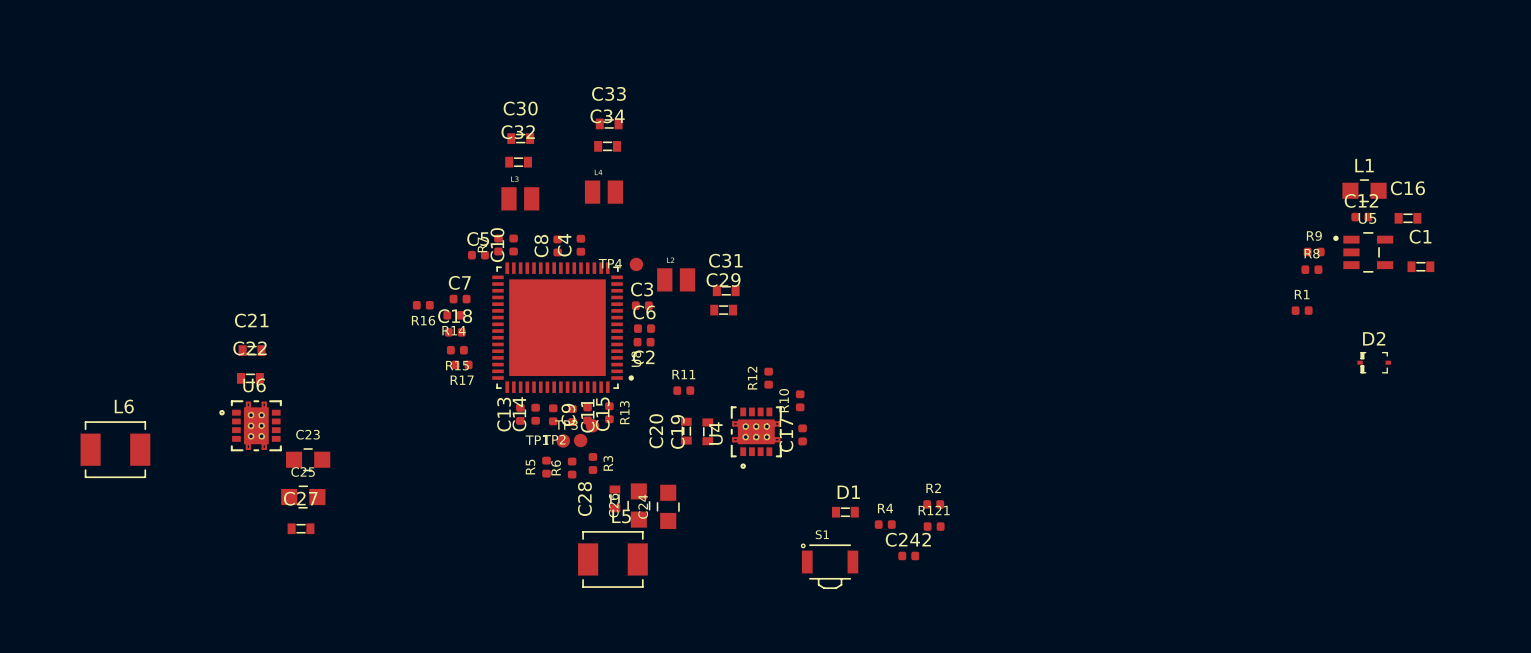
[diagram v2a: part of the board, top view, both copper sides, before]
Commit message: Started PMIC placement
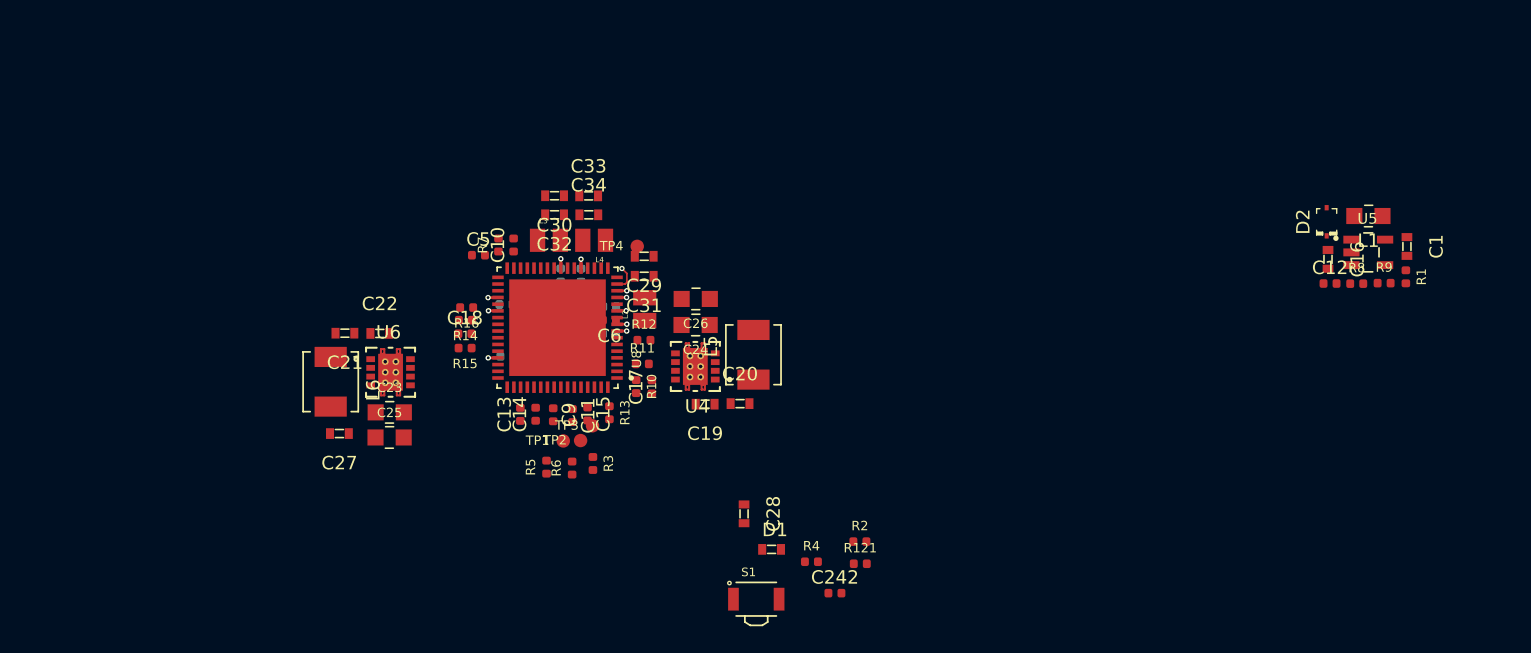
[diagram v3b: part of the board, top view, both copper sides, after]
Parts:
- C2, C3, C4, C7, C8, R17: moved to B.Cu
- moved L5 18.5 mm to (145.1, 136.3), turned to 90 degrees
- moved L6 16.8 mm to (113.6, 138.3), turned to 270 degrees
- moved C26 16.0 mm to (140.8, 132.1), turned to 180 degrees
- moved C24 13.7 mm to (140.8, 134.1), turned to 180 degrees
- moved R10 12.3 mm to (136.3, 138.7), turned to 270 degrees
- moved C17 11.8 mm to (137.5, 138.7)
- moved D2 11.1 mm to (187.8, 126.4), turned to 90 degrees
- moved U6 10.8 mm to (118.0, 137.6)
- moved C22 10.2 mm to (117.2, 134.7)
- moved R12 9.71 mm to (136.9, 135.2), turned to 0 degrees
- moved C28 9.68 mm to (144.4, 148.1), turned to 270 degrees
- moved R1 8.13 mm to (193.7, 130.5), turned to 270 degrees
- moved C25 7.81 mm to (118.0, 142.4)
- moved C27 7.65 mm to (114.2, 142.2), turned to 180 degrees
- moved C29 7.15 mm to (136.9, 128.9), turned to 180 degrees
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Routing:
- net VCC_5V0: track 0.00 -> 3.48 mm, vias 0 -> 5
- net Net-(TP4-Pad1): track 0.00 -> 1.97 mm, vias 0 -> 1
- net GND: track 408.6 -> 410.0 mm, vias 227 -> 229
- net LDO_3V3: track 0.00 -> 0.70 mm, vias 0 -> 1
- net Net-(R17-Pad1): track 0.00 -> 0.70 mm, vias 0 -> 1
- net PWR_EN: track 0.00 -> 0.69 mm, vias 0 -> 1
